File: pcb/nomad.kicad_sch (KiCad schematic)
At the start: 47 parts, among them J1 USB_C_Receptacle_USB2.0_16P, J5 Conn_01x02_Pin, SW1 UP, SW2 DOWN, SW3 RIGHT, SW4 LEFT, SW5 SEL, SW6 SW_Push, SW7 SW_Push, SW8 SW_SPDT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

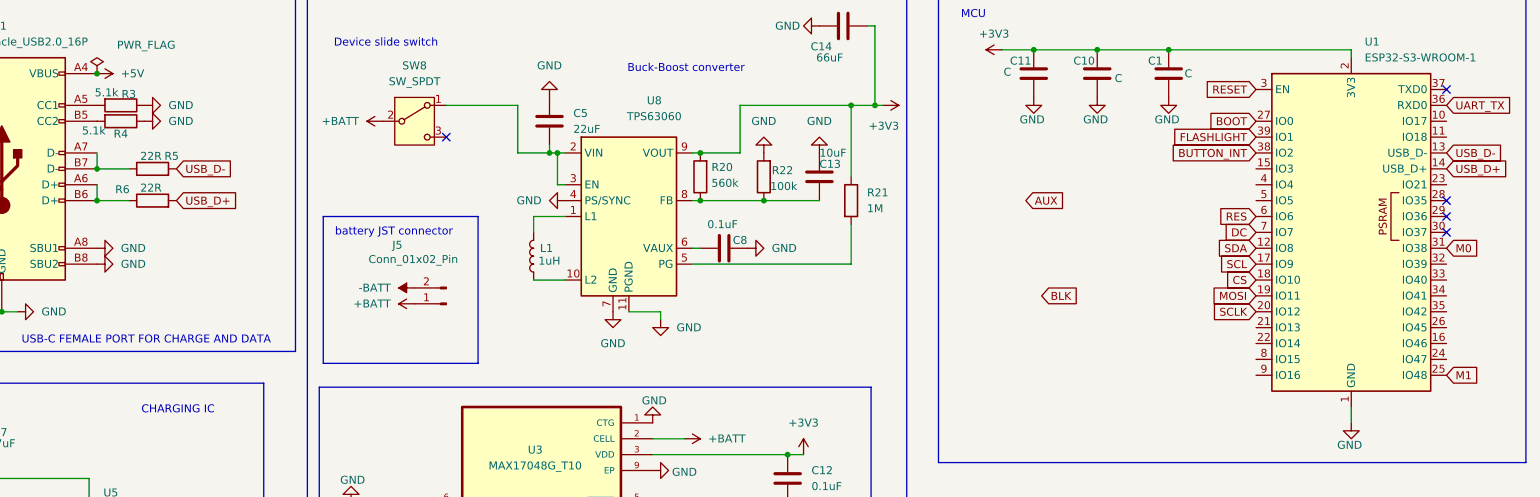
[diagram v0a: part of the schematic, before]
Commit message: Adding LoRa module schematic
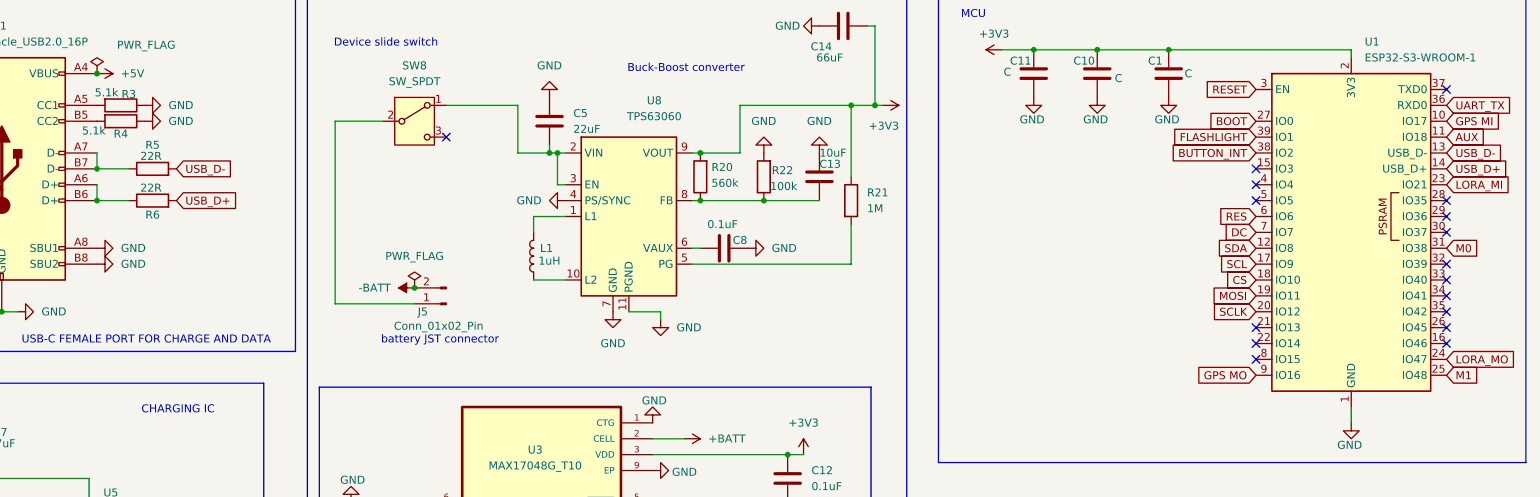
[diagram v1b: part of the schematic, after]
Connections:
- net +BATT: no longer J5.1 (Pin_1), SW8.2 (B)
- net AUX: now also U1.11 (IO18)
- net GPS MI: now reaches U1.10 (IO17)
- net LORA_MI: now reaches U1.23 (IO21)
- net LORA_MO: now reaches U1.24 (IO47)
- net GPS MO: now reaches U1.9 (IO16)
- new net: J5.1 (Pin_1), SW8.2 (B)
- no-connect marks 12 -> 24

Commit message: Finishing schematic and updating PCB
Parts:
- removed C11: C, Capacitor_SMD:C_0805_2012Metric, symbol Device:C
- C1: value C -> 0.1uF
- C10: value C -> 22uF
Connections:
- net -BATT is gone; now on net GND: J5.2 (Pin_2)
- net +BATT: now also J5.1 (Pin_1), SW8.2 (B)
- net at C5.2, U8.2 (VIN), U8.3 (EN): now also SW8.3 (C); no longer SW8.1 (A)
- net UART_TX: no longer names the net of U1.36 (RXD0)
- no-connect marks 24 -> 25
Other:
- moved on the sheet: C12, C13, C14, C2, C3, C4, C5, C7, C8, J5, L1, R15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

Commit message: Routing the PCB
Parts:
- C13: value 10uF -> 10pF
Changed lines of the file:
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@@
 		(rev "[In dev]")
 		(comment 1 "By @0Zane")
-		(comment 2 "Built for @Hackclub, fallout")
 	)
 	(rectangle
@@
 	(wire
 		(pts
-			(xy 29.2661 189.23) (xy 35.6161 189.23)
+			(xy 29.21 189.23) (xy 35.56 189.23)
 		)
 		(stroke
@@
 	(wire
 		(pts
+			(xy 29.1539 181.61) (xy 29.21 181.61)
+		)
+		(stroke
+			(width 0)
+			(type default)
+		)
+	)
+	(wire
+		(pts
 			(xy 139.7 168.91) (xy 140.97 168.91)
 		)
@@
 	(global_label "BTN_DOWN"
 		(shape input)
-		(at 29.2661 189.23 180)
+		(at 29.21 189.23 180)
 		(fields_autoplaced yes)
 		(effects
@@
 		)
 		(property "Intersheetrefs" "${INTERSHEET_REFS}"
-			(at 16.3628 189.23 0)
+			(at 16.3067 189.23 0)
 			(hide yes)
 			(show_name no)
@@
 	(symbol
 		(lib_id "power:GND")
-		(at 45.7761 189.23 90)
+		(at 45.72 189.23 90)
 		(unit 1)
 		(body_style 1)
@@
 		(fields_autoplaced yes)
 		(property "Reference" "#PWR015"
-			(at 52.1261 189.23 0)
+			(at 52.07 189.23 0)
 			(hide yes)
 			(show_name no)
@@
 		)
 		(property "Value" "GND"
-			(at 49.5861 189.2299 90)
+			(at 49.53 189.2299 90)
 			(show_name no)
 			(do_not_autoplace no)
@@
 		)
 		(property "Footprint" ""
-			(at 45.7761 189.23 0)
+			(at 45.72 189.23 0)
 			(hide yes)
 			(show_name no)
@@
 		)
 		(property "Datasheet" ""
-			(at 45.7761 189.23 0)
+			(at 45.72 189.23 0)
 			(hide yes)
 			(show_name no)
@@
 		)
 		(property "Description" "Power symbol creates a global label with name \"GND\" , ground"
-			(at 45.7761 189.23 0)
+			(at 45.72 189.23 0)
 			(hide yes)
 			(show_name no)
@@
 	(symbol
 		(lib_id "power:+3V3")
-		(at 29.2661 181.61 0)
+		(at 29.1539 181.61 0)
 		(unit 1)
 		(body_style 1)
@@
 		(fields_autoplaced yes)
 		(property "Reference" "#PWR014"
-			(at 29.2661 185.42 0)
+			(at 29.1539 185.42 0)
 			(hide yes)
 			(show_name no)
@@
 		)
 		(property "Value" "+3V3"
-			(at 29.2661 176.53 0)
+			(at 29.1539 176.53 0)
 			(show_name no)
 			(do_not_autoplace no)
@@
 		)
 		(property "Footprint" ""
-			(at 29.2661 181.61 0)
+			(at 29.1539 181.61 0)
 			(hide yes)
 			(show_name no)
@@
 		)
 		(property "Datasheet" ""
-			(at 29.2661 181.61 0)
+			(at 29.1539 181.61 0)
 			(hide yes)
 			(show_name no)
@@
 		)
 		(property "Description" "Power symbol creates a global label with name \"+3V3\""
-			(at 29.2661 181.61 0)
+			(at 29.1539 181.61 0)
 			(hide yes)
 			(show_name no)
@@
 			)
 		)
-		(property "Value" "10uF"
-			(at 163.068 55.118 0)
+		(property "Value" "10pF"
+			(at 163.576 55.118 0)
 			(show_name no)
 			(do_not_autoplace no)
@@
 	(symbol
 		(lib_id "Device:R")
-		(at 29.2661 185.42 0)
+		(at 29.21 185.42 0)
 		(unit 1)
 		(body_style 1)
@@
 		(fields_autoplaced yes)
 		(property "Reference" "R8"
-			(at 31.8061 184.1499 0)
+			(at 31.75 184.1499 0)
 			(show_name no)
 			(do_not_autoplace no)
@@
 		)
 		(property "Value" "10k"
-			(at 31.8061 186.6899 0)
+			(at 31.75 186.6899 0)
 			(show_name no)
 			(do_not_autoplace no)
@@
 		)
 		(property "Footprint" "Resistor_SMD:R_0805_2012Metric"
-			(at 27.4881 185.42 90)
+			(at 27.432 185.42 90)
 			(hide yes)
 			(show_name no)
@@
 		)
 		(property "Datasheet" ""
-			(at 29.2661 185.42 0)
+			(at 29.21 185.42 0)
 			(hide yes)
 			(show_name no)
@@
 		)
 		(property "Description" "Resistor"
-			(at 29.2661 185.42 0)
+			(at 29.21 185.42 0)
 			(hide yes)
 			(show_name no)
@@
 		)
 		(property "Sim.Device" ""
-			(at 29.2661 185.42 0)
+			(at 29.21 185.42 0)
 			(hide yes)
 			(show_name no)
@@
 		)
 		(property "Sim.Type" ""
-			(at 29.2661 185.42 0)
+			(at 29.21 185.42 0)
 			(hide yes)
 			(show_name no)
@@
 	(symbol
 		(lib_id "Switch:SW_Push")
-		(at 40.6961 189.23 0)
+		(at 40.64 189.23 0)
 		(unit 1)
 		(body_style 1)
@@
 		(fields_autoplaced yes)
 		(property "Reference" "SW2"
-			(at 40.6961 181.61 0)
+			(at 40.64 181.61 0)
 			(show_name no)
 			(do_not_autoplace no)
@@
 		)
 		(property "Value" "DOWN"
-			(at 40.6961 184.15 0)
+			(at 40.64 184.15 0)
 			(show_name no)
 			(do_not_autoplace no)
@@
 		)
 		(property "Footprint" "Button_Switch_SMD:SW_Push_1P1T_NO_E-Switch_TL3301NxxxxxG"
-			(at 40.6961 184.15 0)
+			(at 40.64 184.15 0)
 			(hide yes)
 			(show_name no)
@@
 		)
 		(property "Datasheet" ""
-			(at 40.6961 184.15 0)
+			(at 40.64 184.15 0)
 			(hide yes)
 			(show_name no)
@@
 		)
 		(property "Description" "Push button switch, generic, two pins"
-			(at 40.6961 189.23 0)
+			(at 40.64 189.23 0)
 			(hide yes)
 			(show_name no)
@@
 		)
 		(property "Sim.Device" ""
-			(at 40.6961 189.23 0)
+			(at 40.64 189.23 0)
 			(hide yes)
 			(show_name no)
@@
 		)
 		(property "Sim.Type" ""
-			(at 40.6961 189.23 0)
+			(at 40.64 189.23 0)
 			(hide yes)
 			(show_name no)

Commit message: Finishing routing
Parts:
- J5: footprint JST_PH_S2B-PH-K_1x02_P2.00mm_Horizontal -> Connector_JST:JST_PH_S2B-PH-K_1x02_P2.00mm_Horizontal
- SW8: footprint Connector_PinHeader_1.00mm:PinHeader_1x03_P1.00mm_Horizontal -> Connector_PinHeader_1.00mm:PinHeader_1x03_P1.00mm_Vertical
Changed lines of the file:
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@@
 			)
 		)
-		(property "Footprint" "JST_PH_S2B-PH-K_1x02_P2.00mm_Horizontal"
+		(property "Footprint" "Connector_JST:JST_PH_S2B-PH-K_1x02_P2.00mm_Horizontal"
 			(at 101.6 66.04 0)
 			(hide yes)
@@
 			)
 		)
-		(property "Footprint" "Connector_PinHeader_1.00mm:PinHeader_1x03_P1.00mm_Horizontal"
+		(property "Footprint" "Connector_PinHeader_1.00mm:PinHeader_1x03_P1.00mm_Vertical"
 			(at 97.79 36.83 0)
 			(hide yes)

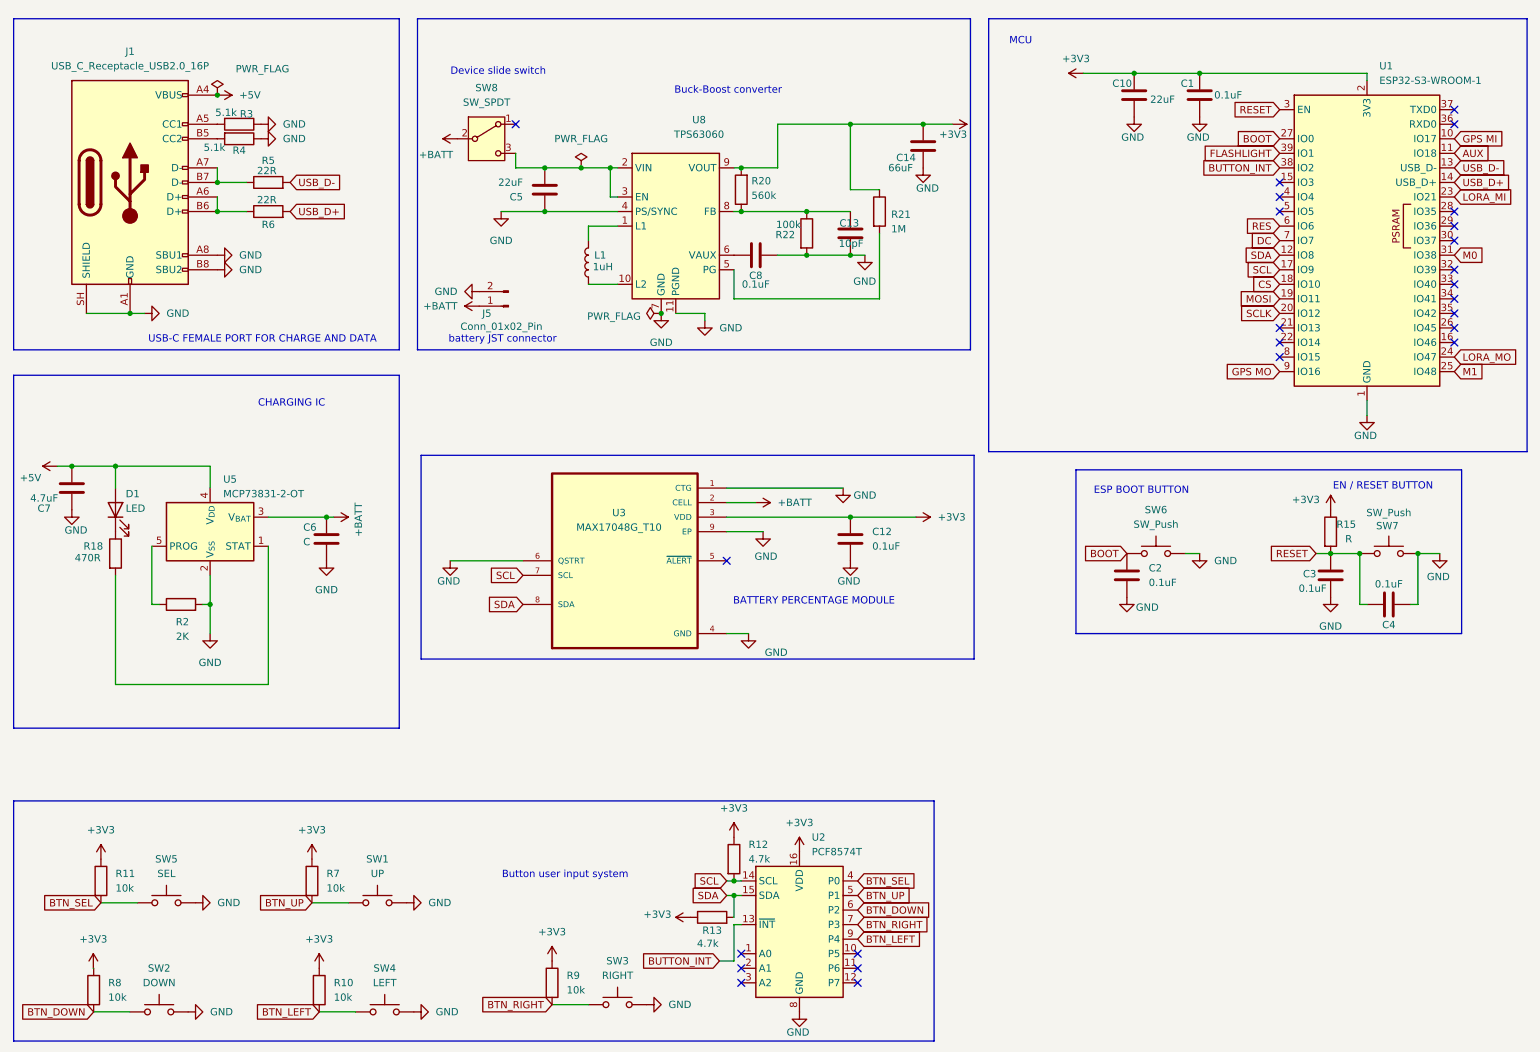
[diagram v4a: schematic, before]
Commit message: Fixing reversed polarity battery connector
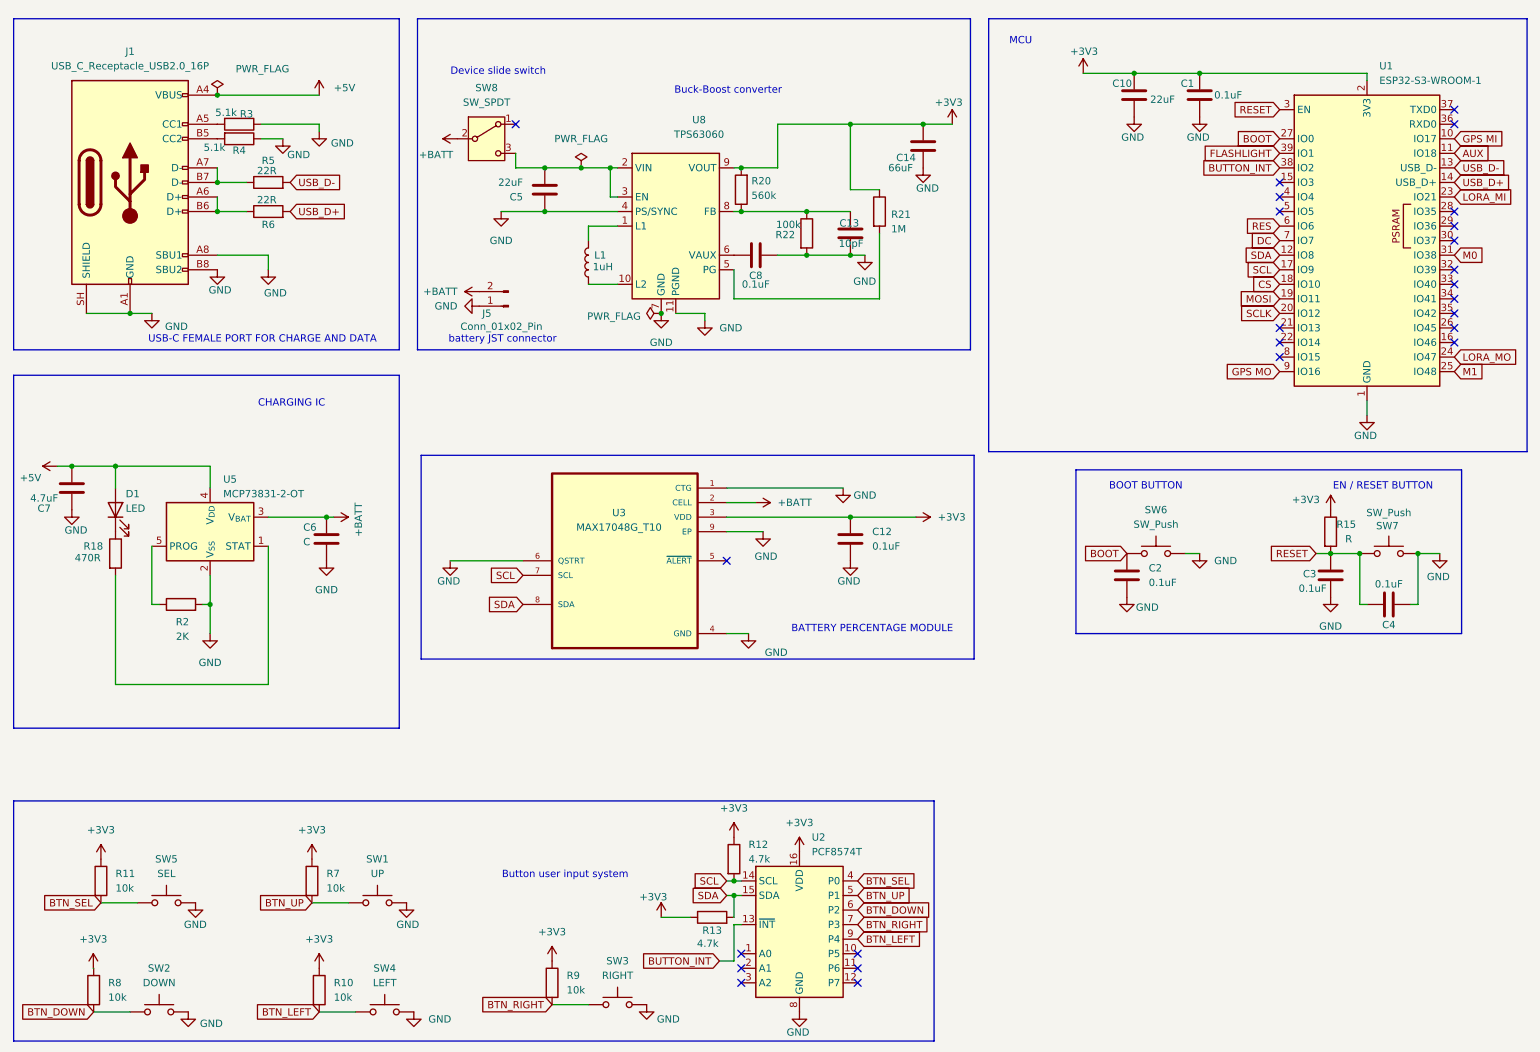
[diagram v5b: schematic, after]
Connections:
- net +BATT: now also J5.2 (Pin_2); no longer J5.1 (Pin_1)
- net GND: now also J5.1 (Pin_1); no longer J5.2 (Pin_2)
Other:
- note added: "BOOT BUTTON"
- note removed: "ESP BOOT BUTTON"

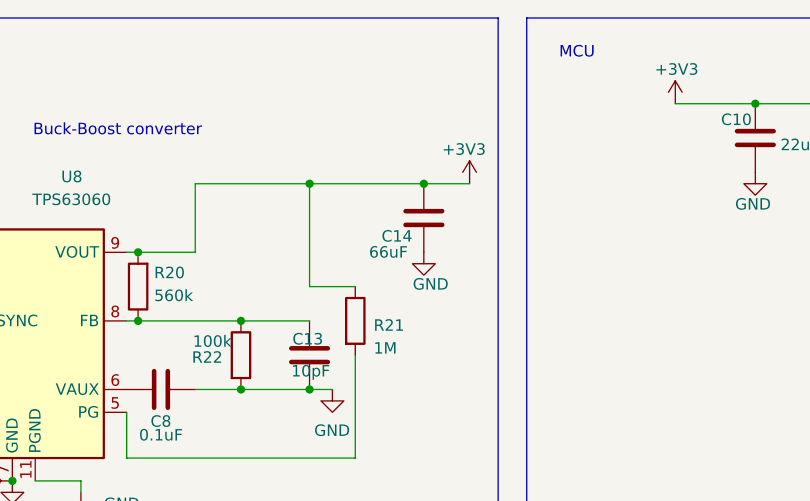
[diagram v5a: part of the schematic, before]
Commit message: Changing 66uF capacitor to 3* 22uF capacitors
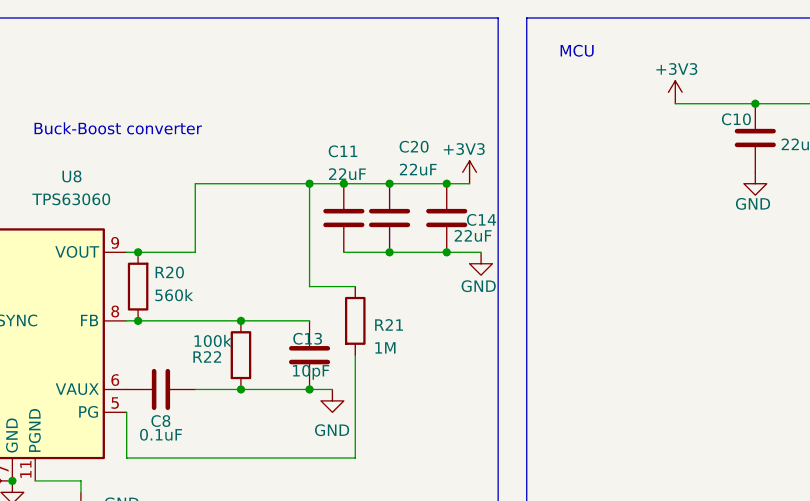
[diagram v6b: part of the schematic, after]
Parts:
- added C11, C20: 22uF, Capacitor_SMD:C_0805_2012Metric, symbol Device:C
- C14: value 66uF -> 22uF
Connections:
- net +3V3: now also C11.1, C20.1
- net GND: now also C11.2, C20.2
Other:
- moved on the sheet: C14

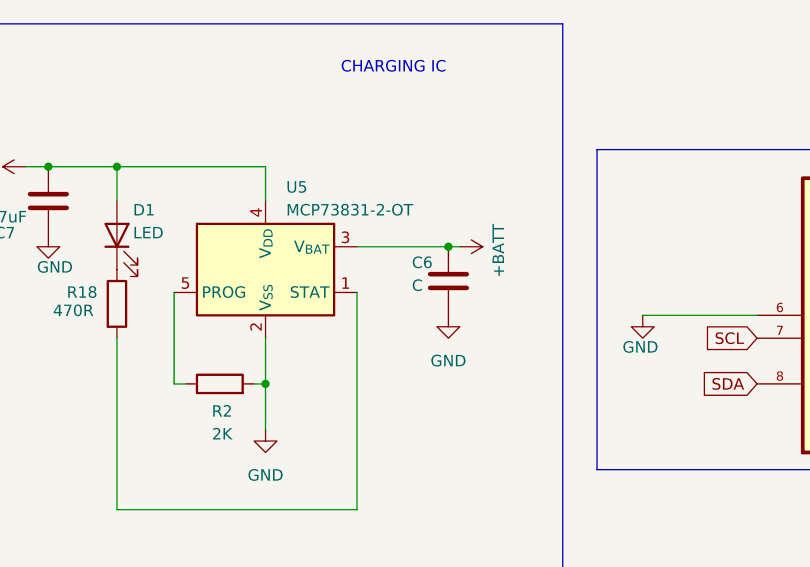
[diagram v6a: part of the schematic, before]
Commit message: Updating bom and adding BOM with every price
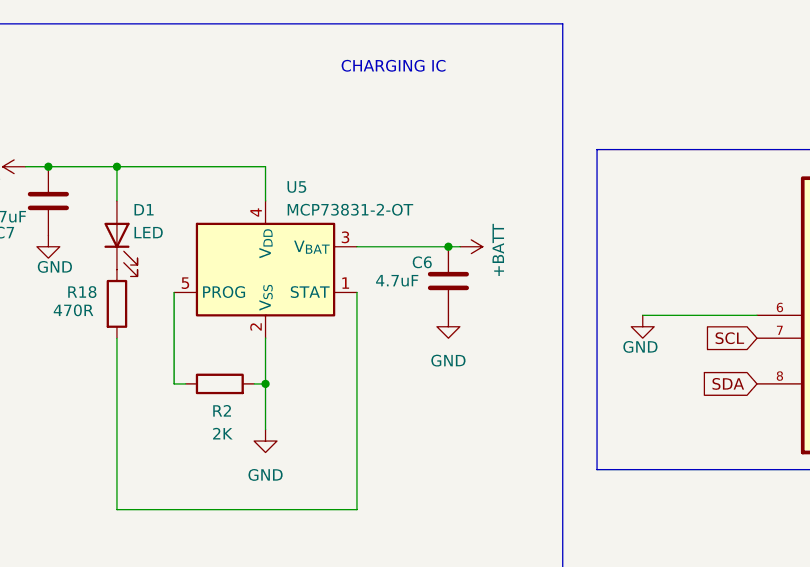
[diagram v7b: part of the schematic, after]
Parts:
- C6: value C -> 4.7uF
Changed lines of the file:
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@@
 			)
 		)
-		(property "Value" "C"
-			(at 65.786 107.188 0)
+		(property "Value" "4.7uF"
+			(at 61.722 106.68 0)
 			(show_name no)
 			(do_not_autoplace no)
